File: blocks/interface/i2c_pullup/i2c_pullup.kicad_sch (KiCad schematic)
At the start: 2 parts

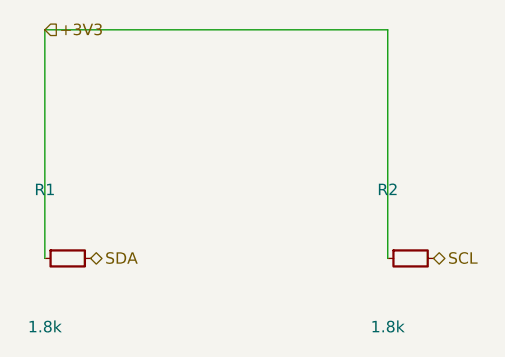
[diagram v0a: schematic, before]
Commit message: i2c_pullup 가독 규칙 소급 (rev 0.2) + R8 자기 핀 스텁 면제
- 1호 블록을 명시 배치로 재작업: +3V3 레일/전압 표기, 스텁 상하 대칭(R11),
  R12 2행 표기, 단위 1.8kΩ(R10), 특성표+리비전(R15), SDA/SCL 하향 라벨.
  전원은 power_in 전역 심볼로 전환 (시트 핀은 신호만 — R15 관례).
- wire_body_hits: 자기 핀에 끝점이 닿는 스텁은 여백(R8) 면제 — 0402처럼
  몸체-핀 간격이 1.27 미만인 소형 수동소자의 구조적 오탐 제거.
  몸체 통과(R3)는 유지. 전 블록 4개 선검증 무회귀.
- 커널 넷리스트 교차검증 3/3 일치.

Co-Authored-By: Claude Fable 5 <noreply@anthropic.com>
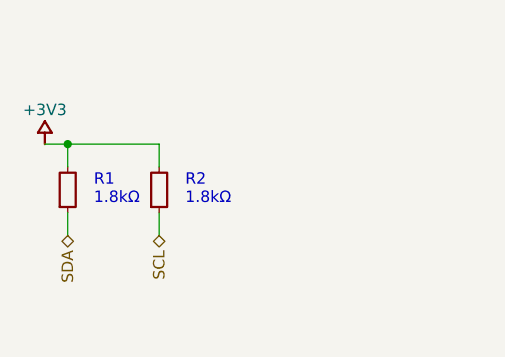
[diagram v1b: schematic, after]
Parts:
- R1, R2: value 1.8k -> 1.8kΩ
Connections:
- net +3V3: now also R1.2, R2.2; no longer R1.1, R2.1
- net SCL: now also R2.1; no longer R2.2
- net SDA: now also R1.1; no longer R1.2
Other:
- note added: "1.8kΩ"
- note added: "R1"
- note added: "R2"
